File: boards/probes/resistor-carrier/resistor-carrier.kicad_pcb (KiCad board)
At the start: 2 copper layers, 7 x 7 mm, 3 parts, among them J1 CONN_01X01, J2 CONN_01X01

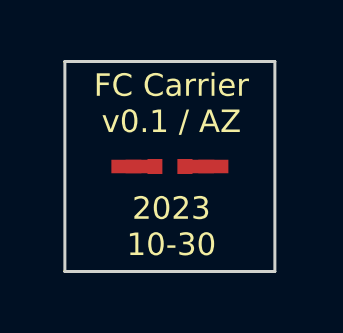
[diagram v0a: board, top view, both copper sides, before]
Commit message: Resistor carrier v0.2 design
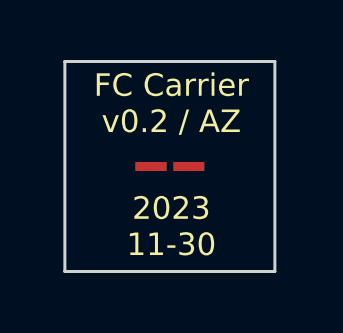
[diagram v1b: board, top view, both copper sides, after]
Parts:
- R1: footprint azonenberg_pcb:EIA_0402_RES_NOSILK_FLIPCHIP -> azonenberg_pcb:EIA_0201_RES_NOSILK
- moved J1 0.60 mm to (89.9, 68.0)
- moved J2 0.60 mm to (91.6, 68.0)
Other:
- board text added: "2023 11-30"
- board text added: "FC Carrier v0.2 / AZ"
- board text removed: "2023 10-30"
- board text removed: "FC Carrier v0.1 / AZ"
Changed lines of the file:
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@@
   (net 2 "Net-(J2-Pad1)")
   (footprint "azonenberg_pcb:EDGELAUNCH_350UM" (layer "F.Cu")
-    (at 89.3 68)
+    (at 89.9 68)
     (property "Sheetfile" "resistor-carrier.kicad_sch")
     (property "Sheetname" "")
@@
       (effects (font (size 1 1) (thickness 0.15)))
     )
-    (pad "1" smd rect locked (at 0 0) (size 1 0.45) (layers "F.Cu" "F.Paste" "F.Mask")
+    (pad "1" smd rect locked (at 0 0) (size 0.6 0.3) (layers "F.Cu" "F.Paste" "F.Mask")
       (net 1 "Net-(J1-Pad1)") (pinfunction "P1") (pintype "passive") (zone_connect 0))
   )
-  (footprint "azonenberg_pcb:EIA_0402_RES_NOSILK_FLIPCHIP" (layer "F.Cu")
+  (footprint "azonenberg_pcb:EIA_0201_RES_NOSILK" (layer "F.Cu")
     (at 90.75 68)
     (property "Sheetfile" "resistor-carrier.kicad_sch")
     (property "Sheetname" "")
-    (solder_paste_margin -0.06)
     (attr through_hole)
-    (fp_text reference "R1" (at 0 1.5) (layer "F.SilkS") hide
-      (effects (font (size 1 1) (thickness 0.15)))
+    (fp_text reference "R1" (at -0.05 0.75) (layer "F.SilkS") hide
+      (effects (font (size 0.508 0.457) (thickness 0.11)))
     )
-    (fp_text value "R" (at 0 3.5) (layer "F.SilkS") hide
-      (effects (font (size 1 1) (thickness 0.15)))
+    (fp_text value "R" (at 0.05 1.5) (layer "F.SilkS") hide
+      (effects (font (size 0.508 0.457) (thickness 0.11)))
     )
-    (pad "1" smd rect locked (at -0.5 0) (size 0.5 0.5) (layers "F.Cu" "F.Paste" "F.Mask")
+    (pad "1" smd rect locked (at -0.22 0) (size 0.21 0.3) (layers "F.Cu" "F.Paste" "F.Mask")
       (net 1 "Net-(J1-Pad1)") (pintype "passive"))
-    (pad "2" smd rect locked (at 0.5 0) (size 0.5 0.5) (layers "F.Cu" "F.Paste" "F.Mask")
+    (pad "2" smd rect locked (at 0.22 0) (size 0.21 0.3) (layers "F.Cu" "F.Paste" "F.Mask")
       (net 2 "Net-(J2-Pad1)") (pintype "passive"))
     (model ":walter:smd_resistors/r_0402.wrl"
       (offset (xyz 0 0 0))
-      (scale (xyz 1 1 1))
+      (scale (xyz 0.5 0.5 0.5))
       (rotate (xyz 0 0 0))
     )
   )
   (footprint "azonenberg_pcb:EDGELAUNCH_350UM" (layer "F.Cu")
-    (at 92.2 68)
+    (at 91.6 68)
     (property "Sheetfile" "resistor-carrier.kicad_sch")
     (property "Sheetname" "")
@@
       (effects (font (size 1 1) (thickness 0.15)))
     )
-    (pad "1" smd rect locked (at 0 0) (size 1 0.45) (layers "F.Cu" "F.Paste" "F.Mask")
+    (pad "1" smd rect locked (at 0 0) (size 0.6 0.3) (layers "F.Cu" "F.Paste" "F.Mask")
       (net 2 "Net-(J2-Pad1)") (pinfunction "P1") (pintype "passive") (zone_connect 0))
   )
@@
   (gr_line (start 87.25 64.5) (end 87.25 71.5) (layer "Edge.Cuts") (width 0.1))
   (gr_line (start 94.25 64.5) (end 87.25 64.5) (layer "Edge.Cuts") (width 0.1))
-  (gr_text "FC Carrier\nv0.1 / AZ" (at 90.8 65.9) (layer "F.SilkS")
+  (gr_text "FC Carrier\nv0.2 / AZ" (at 90.8 65.9) (layer "F.SilkS")
     (effects (font (size 0.75 0.75) (thickness 0.1)))
   )
-  (gr_text "2023\n10-30" (at 90.8 70) (layer "F.SilkS")
+  (gr_text "2023\n11-30" (at 90.8 70) (layer "F.SilkS")
     (effects (font (size 0.75 0.75) (thickness 0.1)))
   )
-  (segment (start 89.3 68) (end 90.25 68) (width 0.45) (layer "F.Cu") (net 1))
-  (segment (start 91.25 68) (end 92.2 68) (width 0.45) (layer "F.Cu") (net 2))
+  (segment (start 89.9 68) (end 90.4 68) (width 0.3) (layer "F.Cu") (net 1))
+  (segment (start 91.6 68) (end 91.1 68) (width 0.3) (layer "F.Cu") (net 2))
   (zone (net 0) (net_name "") (layers *.Mask) (hatch edge 0.508)
     (connect_pads (clearance 0.508))
@@
     (polygon
       (pts
-        (xy 92.8 68.5)
-        (xy 88.7 68.5)
-        (xy 88.7 67.5)
-        (xy 92.8 67.5)
+        (xy 92.1 68.5)
+        (xy 89.4 68.5)
+        (xy 89.4 67.5)
+        (xy 92.1 67.5)
       )
     )
